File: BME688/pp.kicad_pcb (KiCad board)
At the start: 2 copper layers, 12.1 x 23.5 mm, 12 parts, among them J1 Conn_01x03, J2 Conn_01x04, U1 BME688, U2 CH32V003AxMx, U3 AP62250WU-7

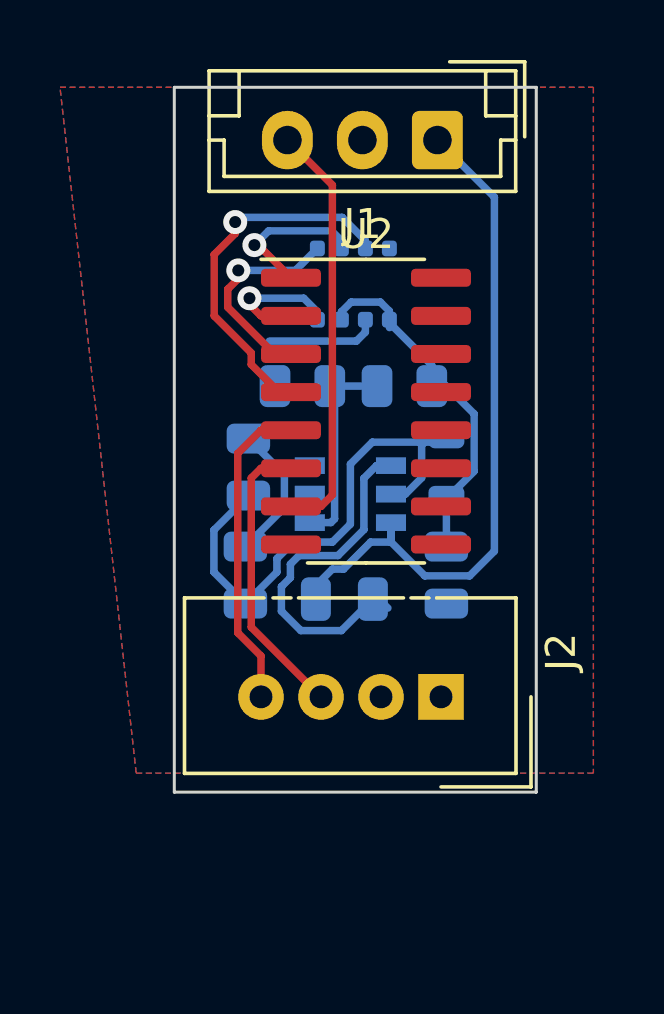
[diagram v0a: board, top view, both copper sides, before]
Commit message: Swap over to STM32 controller
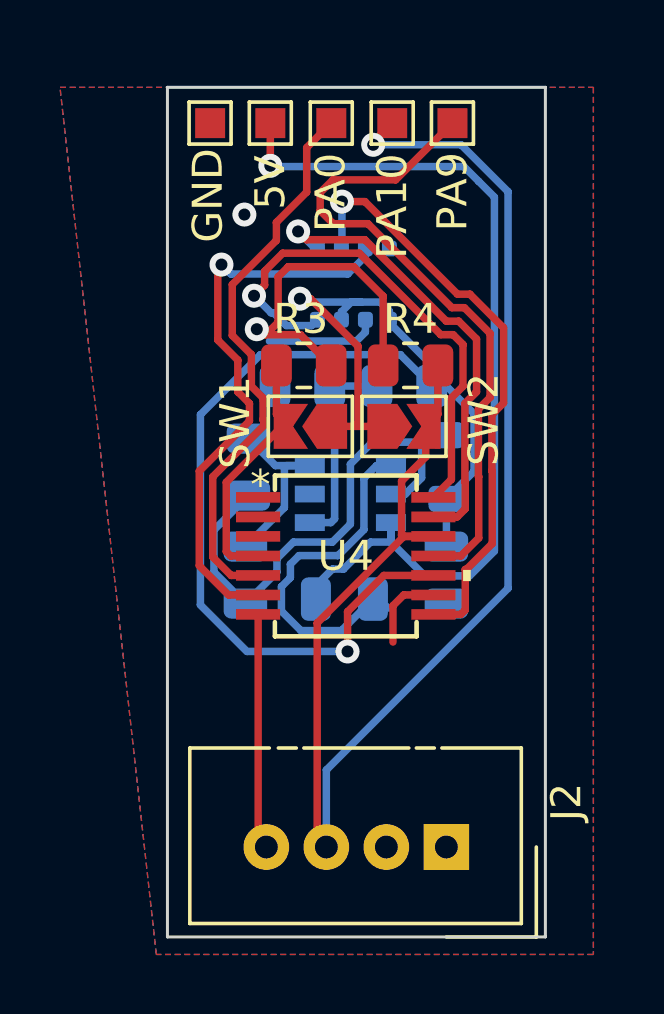
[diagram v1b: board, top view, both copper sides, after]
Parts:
- removed J1: Conn_01x03, Connector_JST:JST_EH_B3B-EH-A_1x03_P2.50mm_Vertical
- removed U2: CH32V003AxMx, Package_SO:SOP-16_3.9x9.9mm_P1.27mm
- added 5V: TestPoint_Pad_1.0x1.0mm, TestPoint:TestPoint_Pad_1.0x1.0mm, F.Cu at (116.2, 67.2)
- added GND: TestPoint_Pad_1.0x1.0mm, TestPoint:TestPoint_Pad_1.0x1.0mm, F.Cu at (114.2, 67.2)
- added PA0: TestPoint_Pad_1.0x1.0mm, TestPoint:TestPoint_Pad_1.0x1.0mm, F.Cu at (118.3, 67.2)
- added PA10: TestPoint_Pad_1.0x1.0mm, TestPoint:TestPoint_Pad_1.0x1.0mm, F.Cu at (120.3, 67.2)
- added PA9: TestPoint_Pad_1.0x1.0mm, TestPoint:TestPoint_Pad_1.0x1.0mm, F.Cu at (122.3, 67.2)
- added R3: 10k, Resistor_SMD:R_0805_2012Metric, F.Cu at (117.3, 75.3)
- added R4: 10k, Resistor_SMD:R_0805_2012Metric, F.Cu at (120.9, 75.3)
- added SW1: SW_SPST, Jumper:SolderJumper-2_P1.3mm_Open_TrianglePad1.0x1.5mm, F.Cu at (117.6, 77.3)
- added SW2: SW_SPST, Jumper:SolderJumper-2_P1.3mm_Open_TrianglePad1.0x1.5mm, F.Cu at (120.7, 77.3)
- added U4: STM32L011D4P6, DOcuments folder:TSSOP14, F.Cu at (118.7, 81.7)
- moved J2 5.01 mm to (122.1, 91.4)
- renumbered 100nF1 to Cx
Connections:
- U1 pad 2: Net-(U1-CSB) -> /CS
- U1 pad 3: Net-(U1-SDI) -> /MOSI
- U1 pad 4: Net-(U1-SCK) -> /CLK
- U1 pad 5: Net-(U1-SDO) -> /MISO
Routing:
- net /Grove2: track 9.72 -> 50.4 mm, vias 0 -> 1
- net +3V3: track 12.1 -> 46.7 mm, vias 0 -> 2
- net /DBG_TX: track 0.00 -> 22.1 mm
- net /MOSI: track 0.00 -> 19.8 mm, vias 0 -> 1
- net /CS: track 0.00 -> 19.0 mm, vias 0 -> 1
- net /DBG_RX: track 0.00 -> 18.7 mm
- net /MISO: track 0.00 -> 17.2 mm, vias 0 -> 1
- net /CLK: track 0.00 -> 15.3 mm, vias 0 -> 1
- net GND: track 15.5 -> 29.7 mm, vias 0 -> 2
- net /SWIO: track 14.0 -> 0.00 mm
- net Net-(U1-CSB): track 12.2 -> 0.00 mm, vias 1 -> 0
- net Net-(SW1-B): track 0.00 -> 8.48 mm
- net Net-(U1-SCK): track 7.07 -> 0.00 mm, vias 1 -> 0
- net +5V: track 23.6 -> 30.2 mm, vias 0 -> 1
- net Net-(U1-SDI): track 5.17 -> 0.00 mm, vias 1 -> 0
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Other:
- board size 12.1 x 23.5 mm -> 12.6 x 28.3 mm
- board text added: "*"

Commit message: Migrate to STM32
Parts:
- added R5: 10k, Resistor_SMD:R_0402_1005Metric, B.Cu at (114.6, 75.9)
- moved J2 1.92 mm to (122.3, 89.5)
- moved C3 0.39 mm to (115.4, 79.1)
- moved C2 0.35 mm to (115.4, 82.7)
- moved SW1 0.25 mm to (117.4, 77.5)
- moved SW2 0.16 mm to (120.7, 77.5)
- renumbered Cx to Cx1
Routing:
- net GND: track 29.7 -> 37.4 mm, vias 2 -> 4
- net /CS: track 19.0 -> 26.1 mm
- net /Grove2: track 50.4 -> 47.1 mm
- net /Grove1: track 7.87 -> 6.04 mm
- net +3V3: track 46.7 -> 47.9 mm
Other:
- board size 12.6 x 28.3 mm -> 12.6 x 26.6 mm

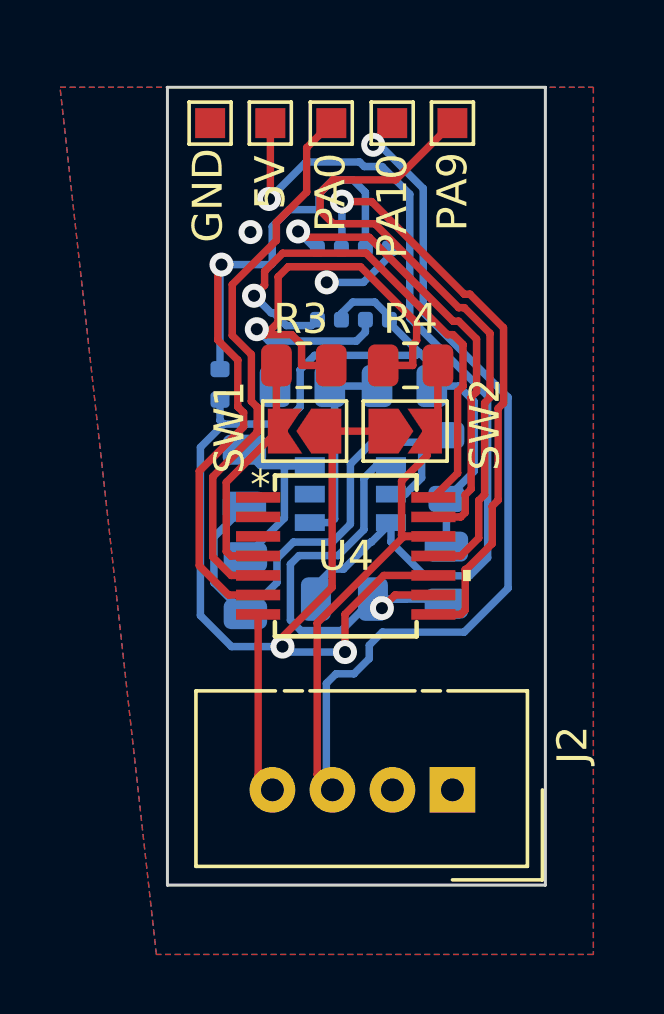
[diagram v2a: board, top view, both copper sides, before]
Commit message: Fix power on BME grove port
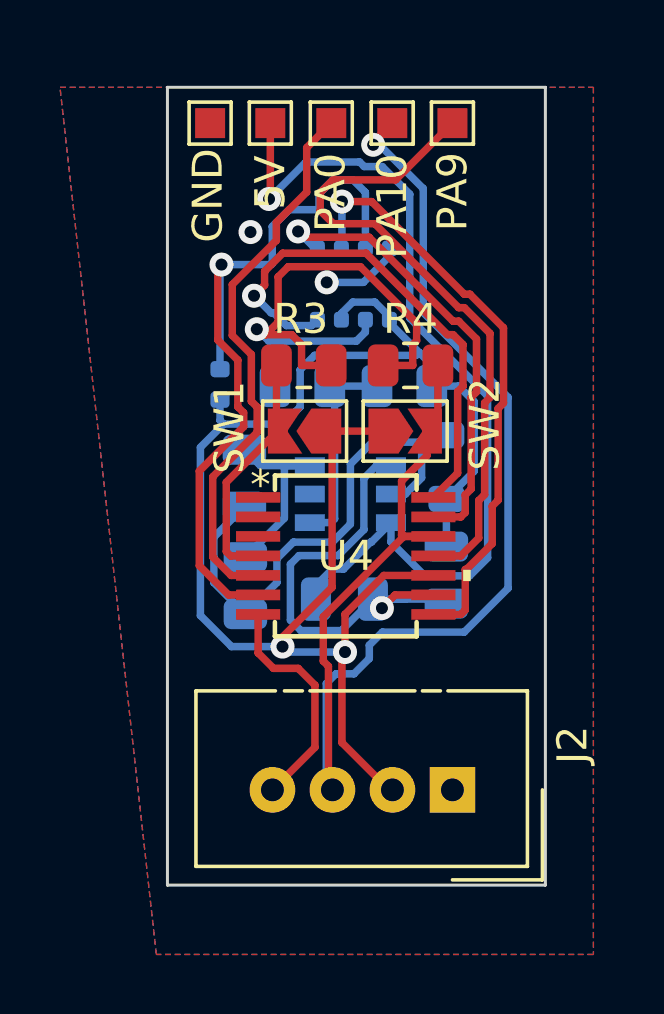
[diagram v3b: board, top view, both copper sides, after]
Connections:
- J2 pad 1: unconnected-(J2-Pin_1-Pad1) -> GND
- J2 pad 2: unconnected-(J2-Pin_2-Pad2) -> +3V3
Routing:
- net +3V3: track 47.9 -> 53.3 mm
- net /Grove1: track 6.04 -> 7.70 mm
